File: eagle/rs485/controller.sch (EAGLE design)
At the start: 47 parts, among them J2 282834-3, J4 JST-XH-04-PIN-ROUND-PAD, U1 AP63203WU-7, U2 SCD-40, U4 ESP32-S3-WROOM-1-N16R2, U5 G3VM-61VY3_TR_, U6 G3VM-61VY3_TR_, U7 RX8111CE_B0, U8 STS35-DIS, U9 SP3485CN-L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

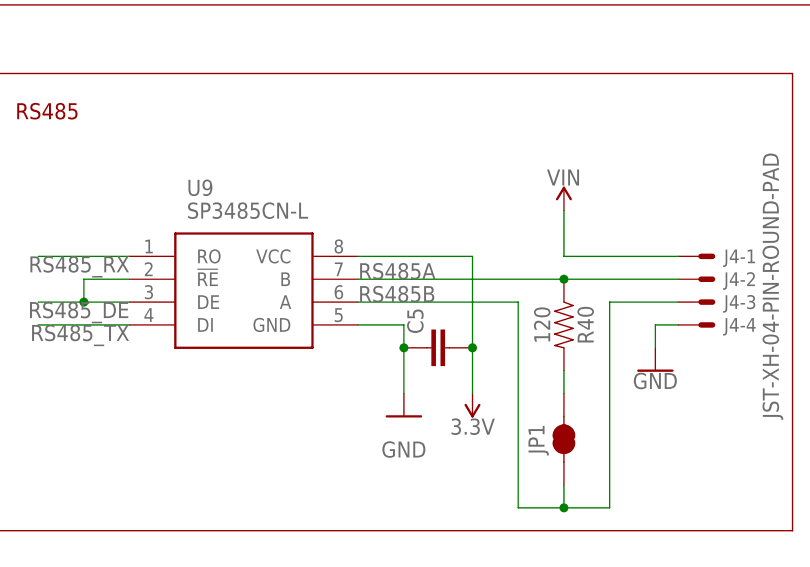
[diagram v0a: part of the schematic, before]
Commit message: finish flipping RS485A/B
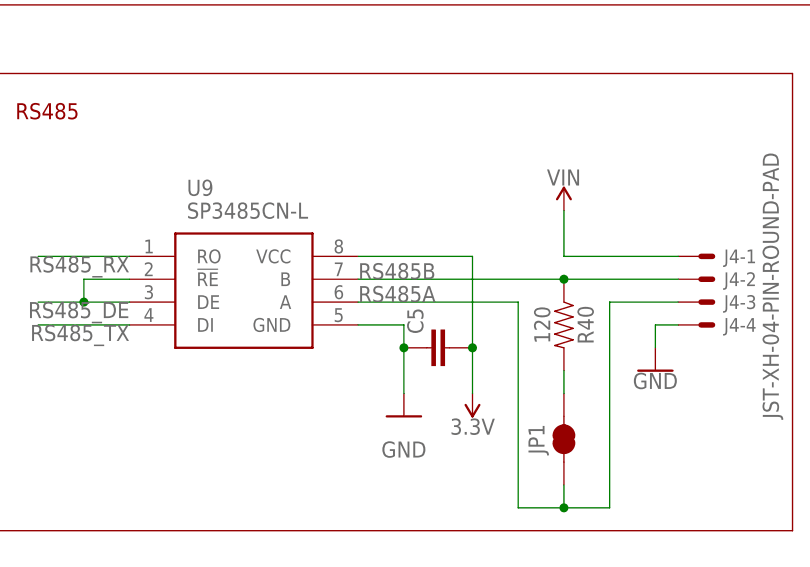
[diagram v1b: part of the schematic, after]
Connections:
- net RS485A: now also J4-3.S, JP1.1, U9.A; no longer J4-2.S, R40.1, U9.B
- net RS485B: now also J4-2.S, R40.1, U9.B; no longer J4-3.S, JP1.1, U9.A
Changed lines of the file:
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@@
 </segment>
 </net>
-<net name="RS485B" class="0">
+<net name="RS485A" class="0">
 <segment>
 <label x="93.98" y="0" size="1.778" layer="95"/>
@@
 </segment>
 </net>
-<net name="RS485A" class="0">
+<net name="RS485B" class="0">
 <segment>
 <wire x1="93.98" y1="2.54" x2="116.84" y2="2.54" width="0.1524" layer="91"/>
